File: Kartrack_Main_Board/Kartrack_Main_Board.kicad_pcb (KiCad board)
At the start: 4 copper layers, 130 x 80 mm, 69 parts, among them IC1 MIC3172YM, J2 Conn_Coaxial, J3 Conn_Coaxial, J4 Conn_01x02_Socket, J5 Conn_01x02_Socket, J6 USB_C_Receptacle_PowerOnly_6P, Q1 RE1C, SW1 SW_Push, SW2 SW_Push, SW3 SW_Push, U2 L76L-M33, U3 Ai-Thinker-Ra-02, U4 BQ21040DBV, U5 BU33SD5WG

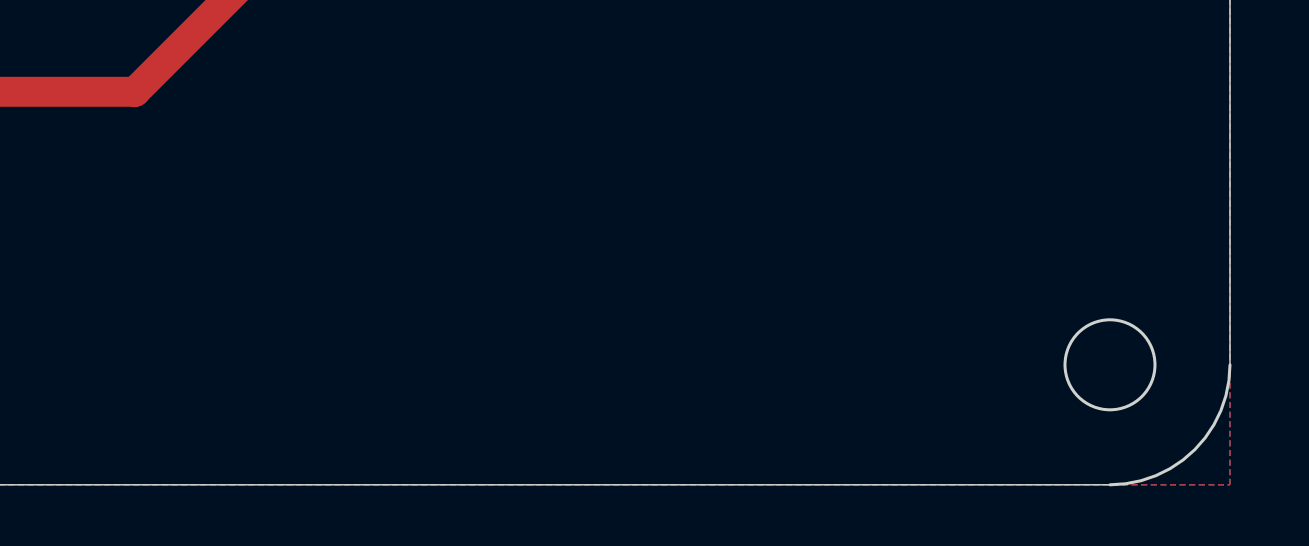
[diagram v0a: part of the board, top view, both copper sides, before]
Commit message: kartrack logo
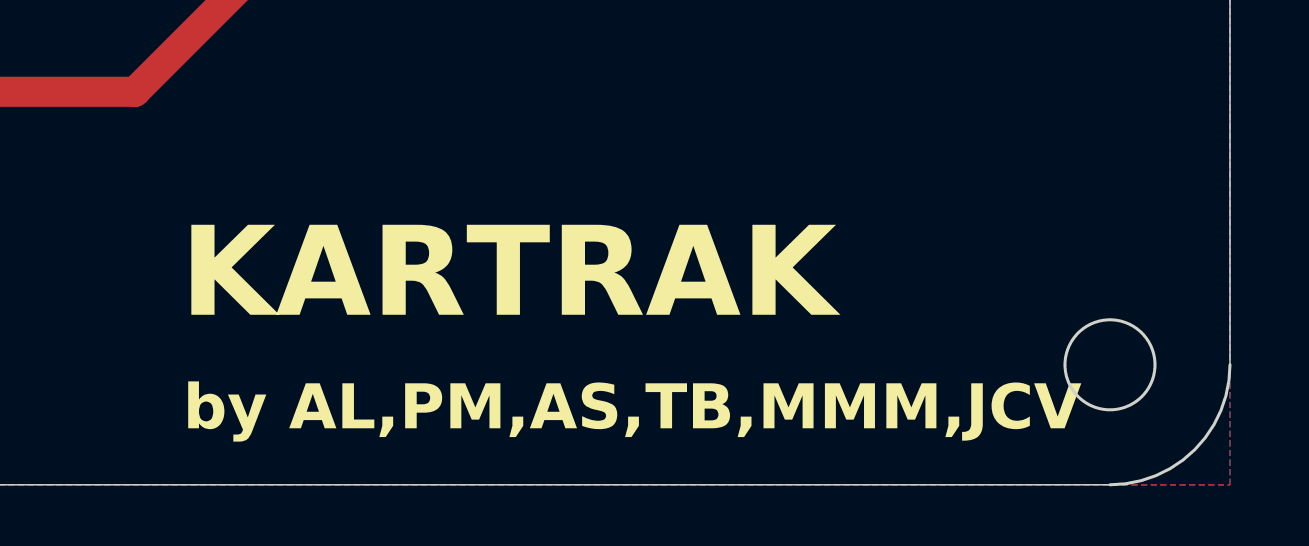
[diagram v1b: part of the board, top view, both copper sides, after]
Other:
- board text added: "KARTRAK"
- board text added: "by AL,PM,AS,TB,MMM,JCV"
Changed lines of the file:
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@@
 		(layer "Edge.Cuts")
+	)
+	(gr_text "by AL,PM,AS,TB,MMM,JCV"
+		(at 190.6 138.8 0)
+		(layer "F.SilkS")
+		(effects
+			(font
+				(size 1.5 1.5)
+				(thickness 0.3)
+				(bold yes)
+			)
+			(justify left bottom)
+		)
+	)
+	(gr_text "KARTRAK "
+		(at 190.5 135.2 0)
+		(layer "F.SilkS")
+		(effects
+			(font
+				(face "Ubuntu")
+				(size 3 3)
+				(thickness 0.6)
+				(bold yes)
+			)
+			(justify left bottom)
+		)
+		(render_cache "KARTRAK " 0
+			(polygon
+				(pts
+					(xy 190.845481 134.69) (xy 190.845481 131.779419) (xy 191.418841 131.779419) (xy 191.418841 132.93658)
+					(xy 191.696362 132.649351) (xy 191.983592 132.345451) (xy 192.256167 132.04778) (xy 192.497051 131.779419)
+					(xy 193.177573 131.779419) (xy 192.879169 132.116474) (xy 192.564279 132.459757) (xy 192.239314 132.79956)
+					(xy 191.91325 133.125441) (xy 192.089323 133.269737) (xy 192.270821 133.438866) (xy 192.446969 133.620912)
+					(xy 192.622531 133.818602) (xy 192.954274 134.242852) (xy 193.252128 134.69) (xy 192.575819 134.69)
+					(xy 192.343178 134.356242) (xy 192.056498 134.007096) (xy 191.740509 133.679933) (xy 191.576429 133.534985)
+					(xy 191.418841 133.41322) (xy 191.418841 134.69)
+				)
+			)
+			(polygon
+				(pts
+					(xy 195.436758 132.406817) (xy 195.714462 133.077814) (xy 196.002241 133.82538) (xy 196.316215 134.69)
+					(xy 195.700907 134.69) (xy 195.586967 134.356608) (xy 195.469914 134.023217) (xy 194.272819 134.023217)
+					(xy 194.154666 134.356608) (xy 194.041826 134.69) (xy 193.446484 134.69) (xy 193.857144 133.563429)
+					(xy 194.410389 133.563429) (xy 195.32923 133.563429) (xy 195.192576 133.190654) (xy 195.065631 132.858911)
+					(xy 194.954806 132.580108) (xy 194.867245 132.365235) (xy 194.785179 132.580108) (xy 194.676003 132.858911)
+					(xy 194.547409 133.190654) (xy 194.410389 133.563429) (xy 193.857144 133.563429) (xy 193.857545 133.56233)
+					(xy 194.23087 132.622056) (xy 194.41787 132.192254) (xy 194.609874 131.779419) (xy 195.152826 131.779419)
+				)
+			)
+			(polygon
+				(pts
+					(xy 197.854939 131.765265) (xy 198.12127 131.812951) (xy 198.335946 131.885664) (xy 198.507807 131.980003)
+					(xy 198.628692 132.081197) (xy 198.721991 132.199923) (xy 198.789941 132.338511) (xy 198.832555 132.500801)
+					(xy 198.847609 132.691849) (xy 198.829623 132.894318) (xy 198.779415 133.059302) (xy 198.699965 133.194317)
+					(xy 198.591474 133.309351) (xy 198.454308 133.407555) (xy 198.283775 133.488874) (xy 198.465858 133.731957)
+					(xy 198.663328 134.031643) (xy 198.855486 134.360272) (xy 199.024014 134.69) (xy 198.383426 134.69)
+					(xy 198.156097 134.290479) (xy 197.918876 133.909827) (xy 197.799809 133.73714) (xy 197.690448 133.598967)
+					(xy 197.660589 133.601165) (xy 197.63073 133.602264) (xy 197.274808 133.602264) (xy 197.274808 134.69)
+					(xy 196.701448 134.69) (xy 196.701448 132.254043) (xy 197.274808 132.254043) (xy 197.274808 133.143393)
+					(xy 197.5058 133.143393) (xy 197.746879 133.132357) (xy 197.923639 133.103459) (xy 198.029695 133.068092)
+					(xy 198.111098 133.02113) (xy 198.1724 132.963325) (xy 198.216754 132.891973) (xy 198.2451 132.801769)
+					(xy 198.255382 132.687636) (xy 198.245105 132.577819) (xy 198.216657 132.490513) (xy 198.171851 132.420922)
+					(xy 198.073851 132.339029) (xy 197.932431 132.280239) (xy 197.768918 132.248746) (xy 197.563503 132.237191)
+					(xy 197.402302 132.243053) (xy 197.274808 132.254043) (xy 196.701448 132.254043) (xy 196.701448 131.824481)
+					(xy 196.905297 131.789047) (xy 197.125148 131.765314) (xy 197.526683 131.747911)
+				)
+			)
+			(polygon
+				(pts
+					(xy 200.048185 134.69) (xy 200.048185 132.268698) (xy 199.157737 132.268698) (xy 199.157737 131.779419)
+					(xy 201.510894 131.779419) (xy 201.510894 132.268698) (xy 200.621545 132.268698) (xy 200.621545 134.69)
+				)
+			)
+			(polygon
+				(pts
+					(xy 203.092483 131.765265) (xy 203.358813 131.812951) (xy 203.573489 131.885664) (xy 203.74535 131.980003)
+					(xy 203.866236 132.081197) (xy 203.959534 132.199923) (xy 204.027484 132.338511) (xy 204.070099 132.500801)
+					(xy 204.085153 132.691849) (xy 204.067167 132.894318) (xy 204.016958 133.059302) (xy 203.937508 133.194317)
+					(xy 203.829018 133.309351) (xy 203.691851 133.407555) (xy 203.521318 133.488874) (xy 203.703401 133.731957)
+					(xy 203.900872 134.031643) (xy 204.09303 134.360272) (xy 204.261557 134.69) (xy 203.620969 134.69)
+					(xy 203.39364 134.290479) (xy 203.15642 133.909827) (xy 203.037353 133.73714) (xy 202.927991 133.598967)
+					(xy 202.898133 133.601165) (xy 202.868274 133.602264) (xy 202.512351 133.602264) (xy 202.512351 134.69)
+					(xy 201.938991 134.69) (xy 201.938991 132.254043) (xy 202.512351 132.254043) (xy 202.512351 133.143393)
+					(xy 202.743344 133.143393) (xy 202.984422 133.132357) (xy 203.161182 133.103459) (xy 203.267238 133.068092)
+					(xy 203.348641 133.02113) (xy 203.409944 132.963325) (xy 203.454297 132.891973) (xy 203.482643 132.801769)
+					(xy 203.492925 132.687636) (xy 203.482649 132.577819) (xy 203.4542 132.490513) (xy 203.409394 132.420922)
+					(xy 203.311395 132.339029) (xy 203.169975 132.280239) (xy 203.006461 132.248746) (xy 202.801046 132.237191)
+					(xy 202.639846 132.243053) (xy 202.512351 132.254043) (xy 201.938991 132.254043) (xy 201.938991 131.824481)
+					(xy 202.142841 131.789047) (xy 202.362691 131.765314) (xy 202.764227 131.747911)
+				)
+			)
+			(polygon
+				(pts
+					(xy 206.506821 132.406817) (xy 206.784525 133.077814) (xy 207.072304 133.82538) (xy 207.386278 134.69)
+					(xy 206.770969 134.69) (xy 206.65703 134.356608) (xy 206.539977 134.023217) (xy 205.342882 134.023217)
+					(xy 205.224729 134.356608) (xy 205.111889 134.69) (xy 204.516547 134.69) (xy 204.927207 133.563429)
+					(xy 205.480451 133.563429) (xy 206.399293 133.563429) (xy 206.262639 133.190654) (xy 206.135694 132.858911)
+					(xy 206.024869 132.580108) (xy 205.937308 132.365235) (xy 205.855242 132.580108) (xy 205.746065 132.858911)
+					(xy 205.617472 133.190654) (xy 205.480451 133.563429) (xy 204.927207 133.563429) (xy 204.927608 133.56233)
+					(xy 205.300933 132.622056) (xy 205.487932 132.192254) (xy 205.679937 131.779419) (xy 206.222889 131.779419)
+				)
+			)
+			(polygon
+				(pts
+					(xy 207.77151 134.69) (xy 207.77151 131.779419) (xy 208.34487 131.779419) (xy 208.34487 132.93658)
+					(xy 208.622391 132.649351) (xy 208.909621 132.345451) (xy 209.182196 132.04778) (xy 209.42308 131.779419)
+					(xy 210.103602 131.779419) (xy 209.805198 132.116474) (xy 209.490308 132.459757) (xy 209.165343 132.79956)
+					(xy 208.839279 133.125441) (xy 209.015352 133.269737) (xy 209.196851 133.438866) (xy 209.372998 133.620912)
+					(xy 209.54856 133.818602) (xy 209.880303 134.242852) (xy 210.178157 134.69) (xy 209.501849 134.69)
+					(xy 209.269207 134.356242) (xy 208.982527 134.007096) (xy 208.666538 133.679933) (xy 208.502458 133.534985)
+					(xy 208.34487 133.41322) (xy 208.34487 134.69)
+				)
+			)
+		)
 	)
 	(segment

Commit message: production files
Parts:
- removed JP3: SolderJumper_2_Open, Jumper:SolderJumper-2_P1.3mm_Open_RoundedPad1.0x1.5mm
- added JP4: SolderJumper_3_Open, Jumper:SolderJumper-3_P2.0mm_Open_TrianglePad1.0x1.5mm_NumberLabels, F.Cu at (198.7, 107.5)
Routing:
- net Net-(A2-VIN): track 3.47 -> 28.1 mm
- net +5V: track 70.1 -> 67.4 mm
- net +3.3V: track 28.4 -> 30.5 mm
- net GND: vias 17 -> 113
